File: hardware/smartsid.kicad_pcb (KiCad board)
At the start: 2 copper layers, 50.8 x 55.9 mm, 63 parts, among them P1 INPUT, P2 CONTROL, P4 SOCKET LEFT, P5 OUTPUT, P6 SOCKET RIGHT, Q1 BC547, Q2 BC547, U1 GAL16V8, U2 SID2, U3 7812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

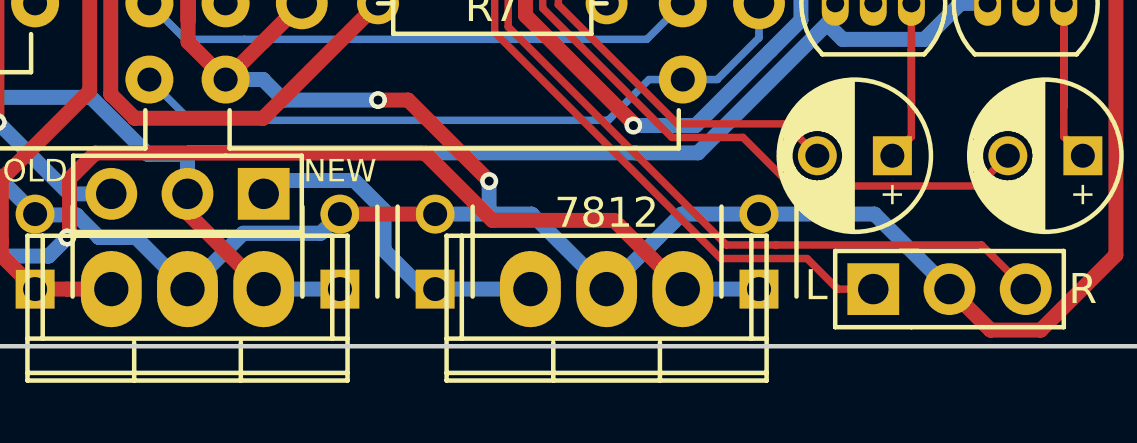
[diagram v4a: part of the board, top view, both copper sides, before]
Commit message: Hardware: Added explicit ground path from power supply to signal ground
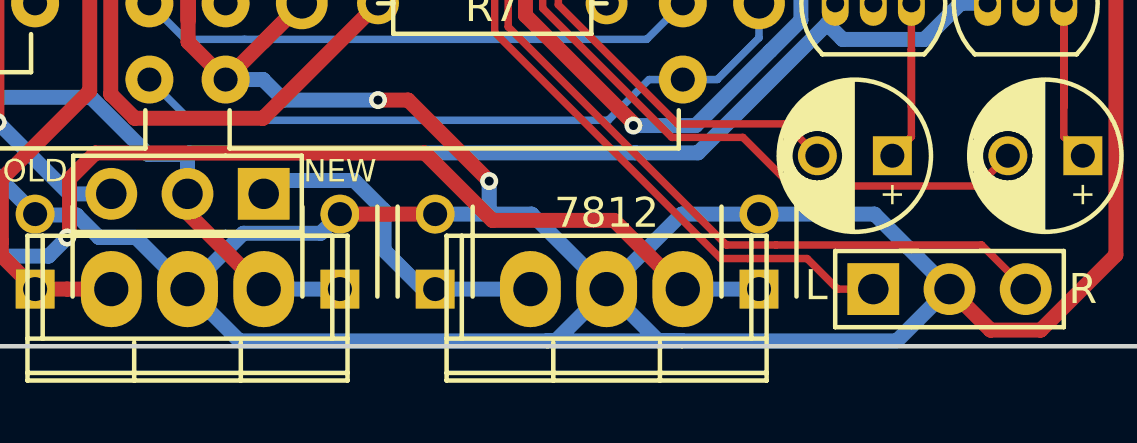
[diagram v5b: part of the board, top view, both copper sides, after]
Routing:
- net GND: track 236.1 -> 268.9 mm
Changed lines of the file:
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@@
     (thickness 1.6)
     (drawings 42)
-    (tracks 995)
+    (tracks 1006)
     (zones 0)
     (modules 63)
@@
   (gr_line (start 179.07 68.58) (end 179.07 67.31) (angle 90) (layer Edge.Cuts) (width 0.15))
   (segment (start 135.509 87.757) (end 132.207 87.757) (width 0.25) (layer B.Cu) (net 1))
-  (segment (start 132.207 87.757) (end 130.81 86.36) (width 0.25) (layer B.Cu) (net 1) (status 800000))
+  (segment (start 132.207 87.757) (end 130.81 86.36) (width 0.25) (layer B.Cu) (net 1))
   (segment (start 140.462 87.757) (end 140.8658 87.3532) (width 0.25) (layer B.Cu) (net 1))
   (segment (start 135.509 87.757) (end 140.462 87.757) (width 0.25) (layer B.Cu) (net 1))
@@
   (segment (start 139.7 85.3847) (end 140.7191 84.3656) (width 0.25) (layer B.Cu) (net 3))
   (segment (start 133.477 84.7953) (end 131.7853 84.7953) (width 0.25) (layer F.Cu) (net 4))
-  (segment (start 131.7853 84.7953) (end 130.81 83.82) (width 0.25) (layer F.Cu) (net 4) (status 800000))
+  (segment (start 131.7853 84.7953) (end 130.81 83.82) (width 0.25) (layer F.Cu) (net 4))
   (segment (start 137.12 86.36) (end 137.12 83.86) (width 0.25) (layer B.Cu) (net 4))
   (segment (start 137.12 83.86) (end 137.16 83.82) (width 0.25) (layer B.Cu) (net 4))
@@
   (segment (start 134.250798 75.819) (end 134.250798 78.967196) (width 0.25) (layer B.Cu) (net 6))
   (segment (start 133.35 74.93) (end 134.1352 75.7152) (width 0.25) (layer B.Cu) (net 6))
+  (segment (start 159.3088 123.0122) (end 163.8046 123.0122) (width 0.5) (layer B.Cu) (net 7))
+  (segment (start 161.29 121.285) (end 161.29 121.3104) (width 0.5) (layer B.Cu) (net 7) (status C00000))
+  (segment (start 161.29 121.3104) (end 159.5882 123.0122) (width 0.5) (layer B.Cu) (net 7) (status 400000))
+  (segment (start 149.0472 123.0122) (end 147.32 121.285) (width 0.5) (layer B.Cu) (net 7) (status 800000))
+  (segment (start 159.5882 123.0122) (end 159.3088 123.0122) (width 0.5) (layer B.Cu) (net 7))
+  (segment (start 159.3088 123.0122) (end 149.0472 123.0122) (width 0.5) (layer B.Cu) (net 7))
+  (segment (start 172.72 121.285) (end 172.6946 121.285) (width 0.5) (layer B.Cu) (net 7) (status C00000))
+  (segment (start 172.6946 121.285) (end 170.9674 123.0122) (width 0.5) (layer B.Cu) (net 7) (status 400000))
+  (segment (start 170.9674 123.0122) (end 163.8046 123.0122) (width 0.5) (layer B.Cu) (net 7))
+  (segment (start 163.0172 123.0122) (end 161.29 121.285) (width 0.5) (layer B.Cu) (net 7) (status 800000))
+  (segment (start 163.8046 123.0122) (end 163.0172 123.0122) (width 0.5) (layer B.Cu) (net 7))
   (segment (start 173.99 72.39) (end 176.53 72.39) (width 0.5) (layer F.Cu) (net 7))
   (segment (start 147.3397 110.8075) (end 147.3397 113.0497) (width 0.5) (layer F.Cu) (net 7))
@@
   (segment (start 153.67 111.76) (end 149.839 115.591) (width 0.5) (layer F.Cu) (net 31))
   (segment (start 134.239 90.3147) (end 131.9353 90.3147) (width 0.25) (layer B.Cu) (net 32))
-  (segment (start 131.9353 90.3147) (end 130.81 91.44) (width 0.25) (layer B.Cu) (net 32) (status 800000))
+  (segment (start 131.9353 90.3147) (end 130.81 91.44) (width 0.25) (layer B.Cu) (net 32))
   (segment (start 145.161 90.3147) (end 147.4647 90.3147) (width 0.25) (layer B.Cu) (net 32))
   (segment (start 147.4647 90.3147) (end 148.59 91.44) (width 0.25) (layer B.Cu) (net 32))
@@
   (segment (start 141.5238 90.3147) (end 145.161 90.3147) (width 0.25) (layer B.Cu) (net 32))
   (segment (start 134.112 92.6901) (end 132.0999 92.6901) (width 0.25) (layer B.Cu) (net 33))
-  (segment (start 132.0999 92.6901) (end 130.81 93.98) (width 0.25) (layer B.Cu) (net 33) (status 800000))
+  (segment (start 132.0999 92.6901) (end 130.81 93.98) (width 0.25) (layer B.Cu) (net 33))
   (segment (start 134.62 92.6901) (end 135.2114 92.6901) (width 0.25) (layer B.Cu) (net 33))
   (segment (start 140.531002 91.572502) (end 141.6486 92.6901) (width 0.25) (layer B.Cu) (net 33))
@@
   (segment (start 145.3274 87.7746) (end 146.5293 87.7746) (width 0.25) (layer F.Cu) (net 34))
   (segment (start 133.731 103.0147) (end 131.9353 103.0147) (width 0.25) (layer B.Cu) (net 35))
-  (segment (start 131.9353 103.0147) (end 130.81 104.14) (width 0.25) (layer B.Cu) (net 35) (status 800000))
+  (segment (start 131.9353 103.0147) (end 130.81 104.14) (width 0.25) (layer B.Cu) (net 35))
   (segment (start 148.59 104.14) (end 151.13 101.6) (width 0.25) (layer F.Cu) (net 35))
   (segment (start 148.59 104.14) (end 148.59 104.1082) (width 0.25) (layer B.Cu) (net 35))
@@
   (segment (start 148.59 104.1082) (end 147.4965 103.0147) (width 0.25) (layer B.Cu) (net 35))
   (segment (start 134.366 105.5547) (end 131.9353 105.5547) (width 0.25) (layer B.Cu) (net 36))
-  (segment (start 131.9353 105.5547) (end 130.81 106.68) (width 0.25) (layer B.Cu) (net 36) (status 800000))
+  (segment (start 131.9353 105.5547) (end 130.81 106.68) (width 0.25) (layer B.Cu) (net 36))
   (segment (start 148.59 106.68) (end 151.13 104.14) (width 0.25) (layer F.Cu) (net 36))
   (segment (start 147.4647 105.5547) (end 134.366 105.5547) (width 0.25) (layer B.Cu) (net 36))
   (segment (start 148.59 106.68) (end 147.4647 105.5547) (width 0.25) (layer B.Cu) (net 36))
   (segment (start 134.493 108.0947) (end 131.9353 108.0947) (width 0.25) (layer B.Cu) (net 37))
-  (segment (start 131.9353 108.0947) (end 130.81 109.22) (width 0.25) (layer B.Cu) (net 37) (status 800000))
+  (segment (start 131.9353 108.0947) (end 130.81 109.22) (width 0.25) (layer B.Cu) (net 37))
   (segment (start 148.59 109.22) (end 151.13 106.68) (width 0.25) (layer F.Cu) (net 37))
   (segment (start 147.4647 108.0947) (end 134.493 108.0947) (width 0.25) (layer B.Cu) (net 37))
   (segment (start 148.59 109.22) (end 147.4647 108.0947) (width 0.25) (layer B.Cu) (net 37))
   (segment (start 136.144 110.6347) (end 131.9353 110.6347) (width 0.25) (layer B.Cu) (net 38))
-  (segment (start 131.9353 110.6347) (end 130.81 111.76) (width 0.25) (layer B.Cu) (net 38) (status 800000))
+  (segment (start 131.9353 110.6347) (end 130.81 111.76) (width 0.25) (layer B.Cu) (net 38))
   (segment (start 148.59 111.76) (end 151.13 109.22) (width 0.25) (layer F.Cu) (net 38))
   (segment (start 147.4647 110.6347) (end 136.144 110.6347) (width 0.25) (layer B.Cu) (net 38))

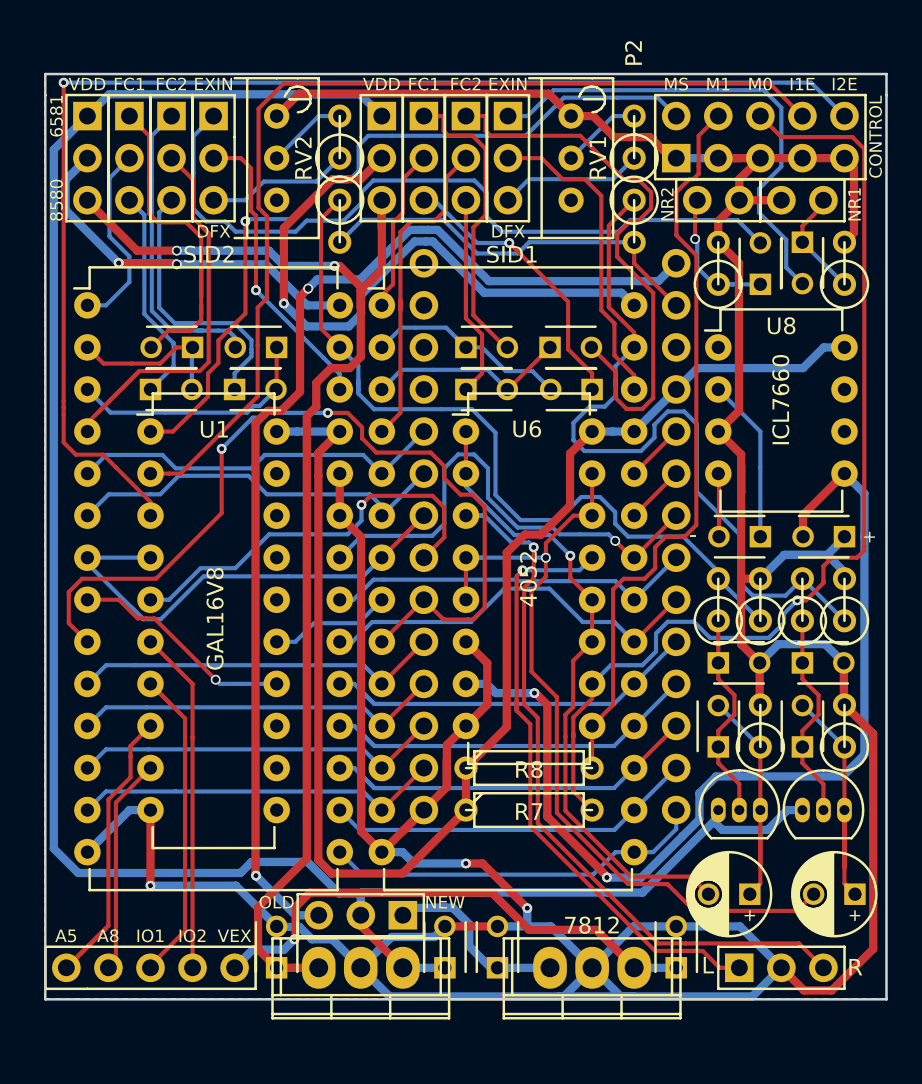
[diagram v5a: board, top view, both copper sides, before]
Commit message: Hardware: Improved routing
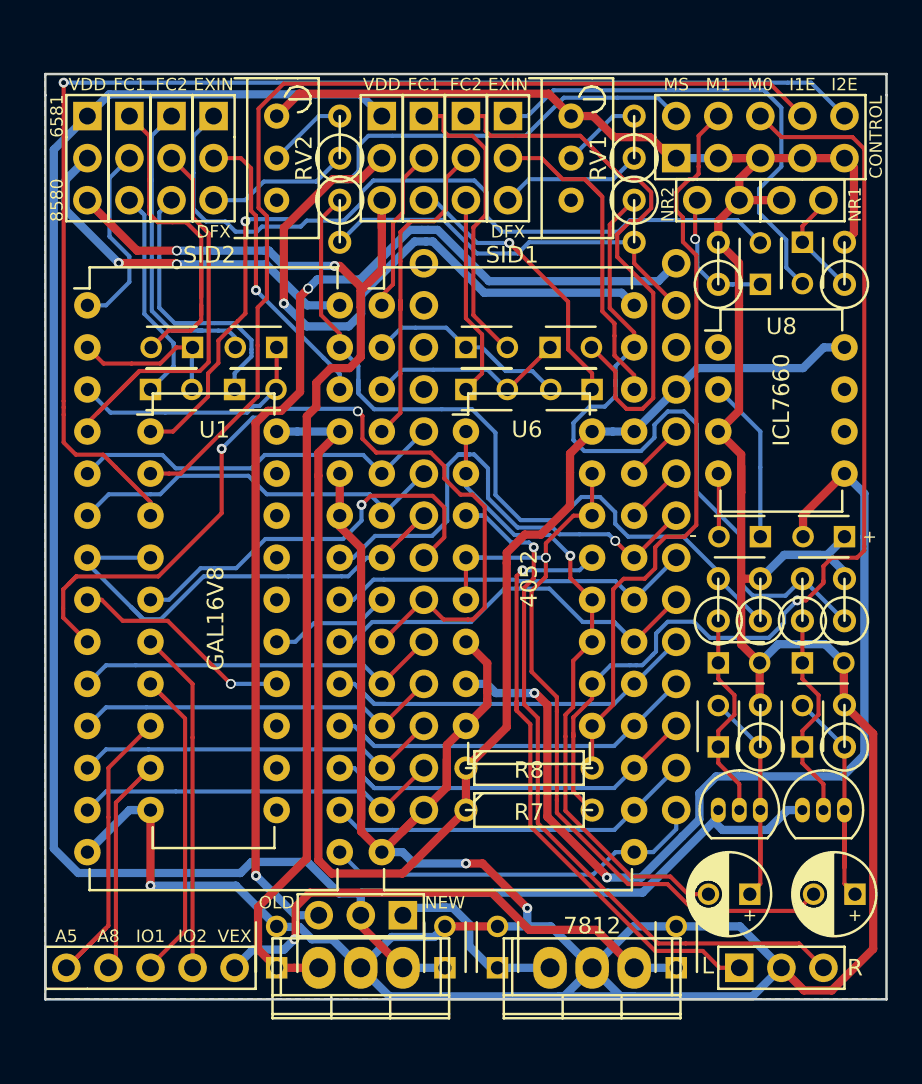
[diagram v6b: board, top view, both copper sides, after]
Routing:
- net /A0: track 53.4 -> 55.3 mm
- net /S1IN: track 19.1 -> 20.5 mm
- net /D7: track 29.6 -> 30.2 mm
